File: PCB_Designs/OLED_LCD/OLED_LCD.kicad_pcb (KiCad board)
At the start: 2 copper layers, 104.1 x 67.8 mm, 27 parts, among them P1 CONN_01X10, P2 CONN_01X16, P3 CONN_01X01, P4 CONN_01X01, P5 CONN_01X01, P6 CONN_01X01, SW1 Rotary_Encoder_Switch, U1 MCP23017, U2 MCP23017, U3 CHERRY-MX

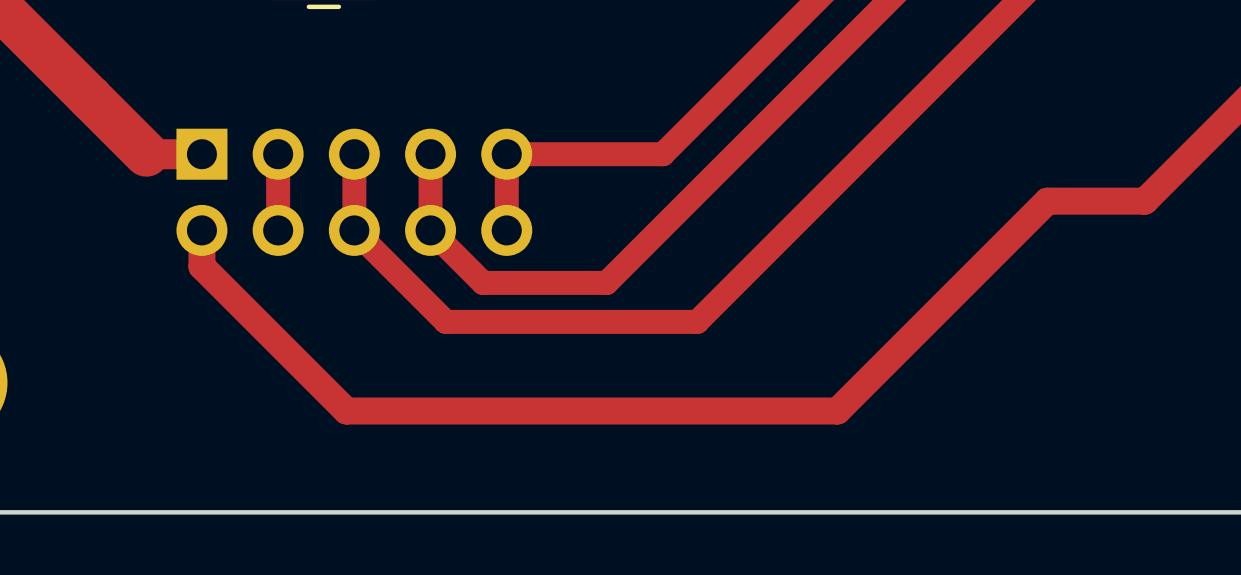
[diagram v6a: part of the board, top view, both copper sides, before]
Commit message: Oled and photomasks
* Added 1k Serie resistance to backlight in Oled LCD.
* Created the photomasks for Buttons and Sliders.
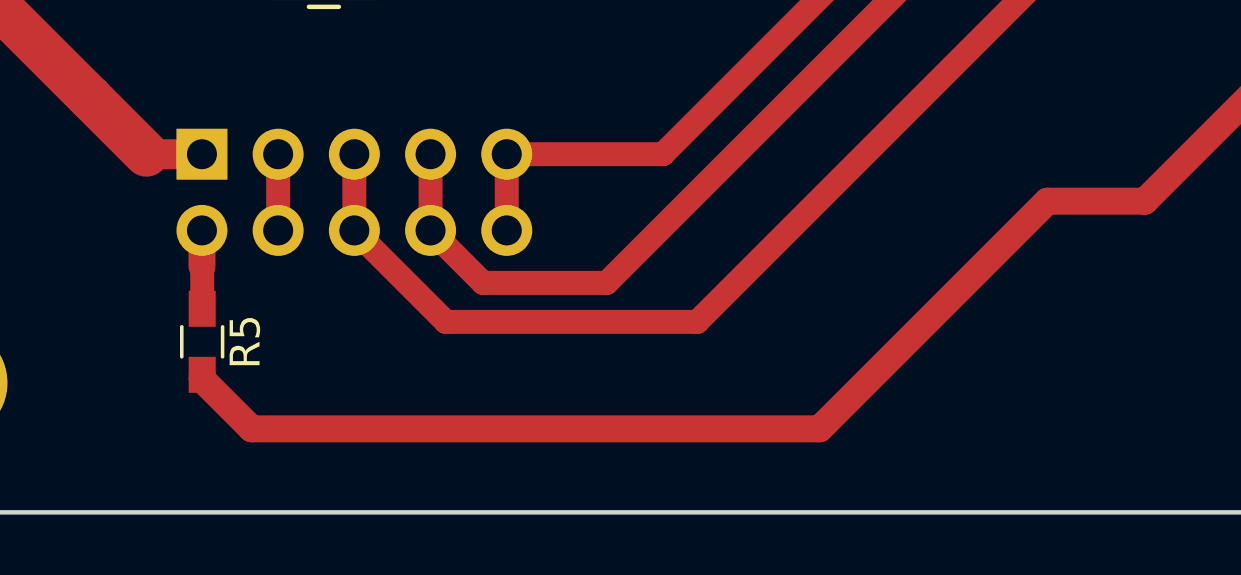
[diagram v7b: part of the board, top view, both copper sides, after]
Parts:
- added R5: 1k, Resistors_SMD:R_0603_HandSoldering, F.Cu at (98.6, 139.3)
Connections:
- P1 pad 2: /LCD_BACKLIGHT -> Net-(P1-Pad2)
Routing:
- net Net-(P1-Pad2): track 0.00 -> 2.62 mm
- net /LCD_BACKLIGHT: track 93.2 -> 91.1 mm
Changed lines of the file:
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@@
 (kicad_pcb (version 4) (host pcbnew 4.0.4-stable)
   (general
-    (links 71)
-    (no_connects 1)
+    (links 72)
+    (no_connects 2)
     (area 86.538999 77.140999 190.829001 145.109001)
     (thickness 1.6)
     (drawings 10)
-    (tracks 315)
+    (tracks 319)
     (zones 0)
-    (modules 27)
-    (nets 53)
+    (modules 28)
+    (nets 54)
   )
   (page A4)
@@
   )
   (setup
-    (last_trace_width 0.8)
+    (last_trace_width 0.9)
     (user_trace_width 0.6)
     (user_trace_width 0.7)
@@
   (net 51 "Net-(U2-Pad27)")
   (net 52 "Net-(U2-Pad28)")
+  (net 53 "Net-(P1-Pad2)")
   (net_class Default "This is the default net class."
     (clearance 0.5)
@@
     (add_net "Net-(C1-Pad1)")
     (add_net "Net-(D1-Pad2)")
+    (add_net "Net-(P1-Pad2)")
     (add_net "Net-(P2-Pad3)")
     (add_net "Net-(P3-Pad1)")
@@
       (net 1 /VCC5))
     (pad 2 thru_hole circle (at 0 2.54) (size 1.7 1.7) (drill 1) (layers *.Cu *.Mask)
-      (net 24 /LCD_BACKLIGHT))
+      (net 53 "Net-(P1-Pad2)"))
     (pad 3 thru_hole circle (at 2.54 0) (size 1.7 1.7) (drill 1) (layers *.Cu *.Mask)
       (net 9 GND))
@@
       (scale (xyz 1 1 1))
       (rotate (xyz 0 0 90))
+    )
+  )
+  (module Resistors_SMD:R_0603_HandSoldering (layer F.Cu)
+    (at 98.56 139.35 270)
+    (descr "Resistor SMD 0603, hand soldering")
+    (tags "resistor 0603")
+    (attr smd)
+    (fp_text reference R5 (at 0 -1.45 270) (layer F.SilkS)
+      (effects (font (size 1 1) (thickness 0.15)))
+    )
+    (fp_text value 1k (at 0 1.55 270) (layer F.Fab)
+      (effects (font (size 1 1) (thickness 0.15)))
+    )
+    (fp_text user %R (at 0 -1.45 270) (layer F.Fab)
+      (effects (font (size 1 1) (thickness 0.15)))
+    )
+    (fp_line (start -0.8 0.4) (end -0.8 -0.4) (layer F.Fab) (width 0.1))
+    (fp_line (start 0.8 0.4) (end -0.8 0.4) (layer F.Fab) (width 0.1))
+    (fp_line (start 0.8 -0.4) (end 0.8 0.4) (layer F.Fab) (width 0.1))
+    (fp_line (start -0.8 -0.4) (end 0.8 -0.4) (layer F.Fab) (width 0.1))
+    (fp_line (start 0.5 0.68) (end -0.5 0.68) (layer F.SilkS) (width 0.12))
+    (fp_line (start -0.5 -0.68) (end 0.5 -0.68) (layer F.SilkS) (width 0.12))
+    (fp_line (start -1.96 -0.7) (end 1.95 -0.7) (layer F.CrtYd) (width 0.05))
+    (fp_line (start -1.96 -0.7) (end -1.96 0.7) (layer F.CrtYd) (width 0.05))
+    (fp_line (start 1.95 0.7) (end 1.95 -0.7) (layer F.CrtYd) (width 0.05))
+    (fp_line (start 1.95 0.7) (end -1.96 0.7) (layer F.CrtYd) (width 0.05))
+    (pad 1 smd rect (at -1.1 0 270) (size 1.2 0.9) (layers F.Cu F.Paste F.Mask)
+      (net 53 "Net-(P1-Pad2)"))
+    (pad 2 smd rect (at 1.1 0 270) (size 1.2 0.9) (layers F.Cu F.Paste F.Mask)
+      (net 24 /LCD_BACKLIGHT))
+    (model Resistors_SMD.3dshapes/R_0603.wrl
+      (at (xyz 0 0 0))
+      (scale (xyz 1 1 1))
+      (rotate (xyz 0 0 0))
     )
   )
@@
   (segment (start 101.516 127.508) (end 101.516 124.376) (width 0.7) (layer F.Cu) (net 23))
   (segment (start 101.516 124.376) (end 101.346 124.206) (width 0.7) (layer F.Cu) (net 23))
+  (segment (start 119.33 142.0614) (end 126.730201 134.661199) (width 0.9) (layer F.Cu) (net 24))
+  (segment (start 100.21 142.25) (end 119.1414 142.25) (width 0.9) (layer F.Cu) (net 24))
+  (segment (start 119.1414 142.25) (end 119.33 142.0614) (width 0.9) (layer F.Cu) (net 24))
+  (segment (start 98.56 140.45) (end 98.56 140.6) (width 0.9) (layer F.Cu) (net 24))
+  (segment (start 98.56 140.6) (end 100.21 142.25) (width 0.9) (layer F.Cu) (net 24))
+  (segment (start 126.730201 134.661199) (end 129.981401 134.661199) (width 0.9) (layer F.Cu) (net 24))
+  (segment (start 129.981401 134.661199) (end 137.7696 126.873) (width 0.9) (layer F.Cu) (net 24))
   (segment (start 139.065 97.2566) (end 139.065 125.5776) (width 1.5) (layer B.Cu) (net 24))
   (segment (start 140.58188 95.73972) (end 139.065 97.2566) (width 2) (layer F.Cu) (net 24))
@@
   (via (at 139.065 125.5776) (size 1.2) (drill 0.8) (layers F.Cu B.Cu) (net 24))
   (segment (start 137.7696 126.873) (end 139.065 125.5776) (width 2) (layer F.Cu) (net 24))
-  (segment (start 129.981401 134.661199) (end 137.7696 126.873) (width 0.9) (layer F.Cu) (net 24))
-  (segment (start 126.730201 134.661199) (end 129.981401 134.661199) (width 0.9) (layer F.Cu) (net 24))
-  (segment (start 98.552 135.636) (end 98.552 136.838081) (width 0.9) (layer F.Cu) (net 24))
-  (segment (start 98.552 136.838081) (end 103.369719 141.6558) (width 0.9) (layer F.Cu) (net 24))
-  (segment (start 119.7356 141.6558) (end 126.730201 134.661199) (width 0.9) (layer F.Cu) (net 24))
-  (segment (start 103.369719 141.6558) (end 119.7356 141.6558) (width 0.9) (layer F.Cu) (net 24))
   (segment (start 110.914 117.602) (end 110.5838 117.2718) (width 0.7) (layer F.Cu) (net 25))
   (segment (start 110.5838 117.2718) (end 108.712 117.2718) (width 0.7) (layer F.Cu) (net 25))
@@
   (segment (start 119.464 115.824) (end 117.686 117.602) (width 0.7) (layer F.Cu) (net 27))
   (segment (start 179.766 87.298082) (end 180.019319 87.551401) (width 0.9) (layer F.Cu) (net 28))
+  (segment (start 98.552 136.838081) (end 98.56 136.846081) (width 0.8) (layer F.Cu) (net 53))
+  (segment (start 98.56 136.846081) (end 98.56 138.25) (width 0.8) (layer F.Cu) (net 53))
+  (segment (start 98.552 135.636) (end 98.552 136.838081) (width 0.9) (layer F.Cu) (net 53))
   (zone (net 9) (net_name GND) (layer F.Cu) (hatch edge 0.508)
     (connect_pads (clearance 0.508))

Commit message: Hej
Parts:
- removed U1: MCP23017, Housings_SOIC:SOIC-28W_7.5x17.9mm_Pitch1.27mm
- moved R5 42.7 mm to (140.9, 134.1), turned to 0 degrees
- moved 10k1 15.3 mm to (85.0, 87.5)
- moved 10k3 15.3 mm to (90.1, 87.5)
- moved SW1 15.3 mm to (87.6, 98.5)
- moved U3 15.1 mm to (87.6, 120.4)
- moved D1 15.1 mm to (87.6, 120.4)
- moved R2 11.0 mm to (91.8, 129.5)
- moved P6 9.91 mm to (82.5, 134.4)
- moved P3 8.46 mm to (82.0, 81.8)
- moved P1 8.22 mm to (105.0, 127.9)
- moved 10k4 7.72 mm to (105.7, 89.8)
- moved 100n2 7.72 mm to (110.2, 89.8)
- moved R3 7.47 mm to (104.6, 117.0)
- moved C1 7.47 mm to (104.7, 120.7)
- moved R1 7.47 mm to (104.6, 118.9)
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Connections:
- U2 pad 18: Net-(U2-Pad18) -> /VCC5
- U2 pad 20: Net-(U2-Pad20) -> /INTA
- U2 pad 21: Net-(U2-Pad21) -> /BUTT_LED
- U2 pad 22: Net-(U2-Pad22) -> /BUTTON_2
- U2 pad 23: /RS -> /ENCODERSW
- U2 pad 24: /RW -> /ENCODERB
- U2 pad 25: /E -> /ENCODERA
- U2 pad 26: Net-(U2-Pad26) -> /RS
- U2 pad 27: Net-(U2-Pad27) -> /RW
- U2 pad 28: Net-(U2-Pad28) -> /E
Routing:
- net GND: track 190.3 -> 519.4 mm, vias 11 -> 12
- net /VCC5: track 297.7 -> 404.0 mm
- net /ENCODERSW: track 23.7 -> 72.9 mm
- net /BUTT_LED: track 23.8 -> 64.5 mm, vias 0 -> 2
- net /LCD_BACKLIGHT: track 91.1 -> 50.7 mm
- net /BUTTON_2: track 6.24 -> 41.6 mm
- net Net-(P1-Pad2): track 2.62 -> 37.0 mm
- net /ENCODERB: track 22.9 -> 57.2 mm
- net /ENCODERA: track 26.6 -> 60.8 mm
- net /SDA#: track 72.5 -> 58.5 mm, vias 0 -> 2
- net /SCL#: track 79.5 -> 69.5 mm, vias 0 -> 2
- net Net-(10k3-Pad1): track 10.6 -> 19.2 mm
- net Net-(10k1-Pad2): track 17.0 -> 24.9 mm
- net Net-(R1-Pad2): track 4.91 -> 12.6 mm
- net /E: track 46.5 -> 42.0 mm
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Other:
- board size 104.1 x 67.8 mm -> 110 x 69.5 mm
